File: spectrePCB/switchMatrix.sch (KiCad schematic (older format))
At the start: 259 parts, among them U2 ADG633YRU

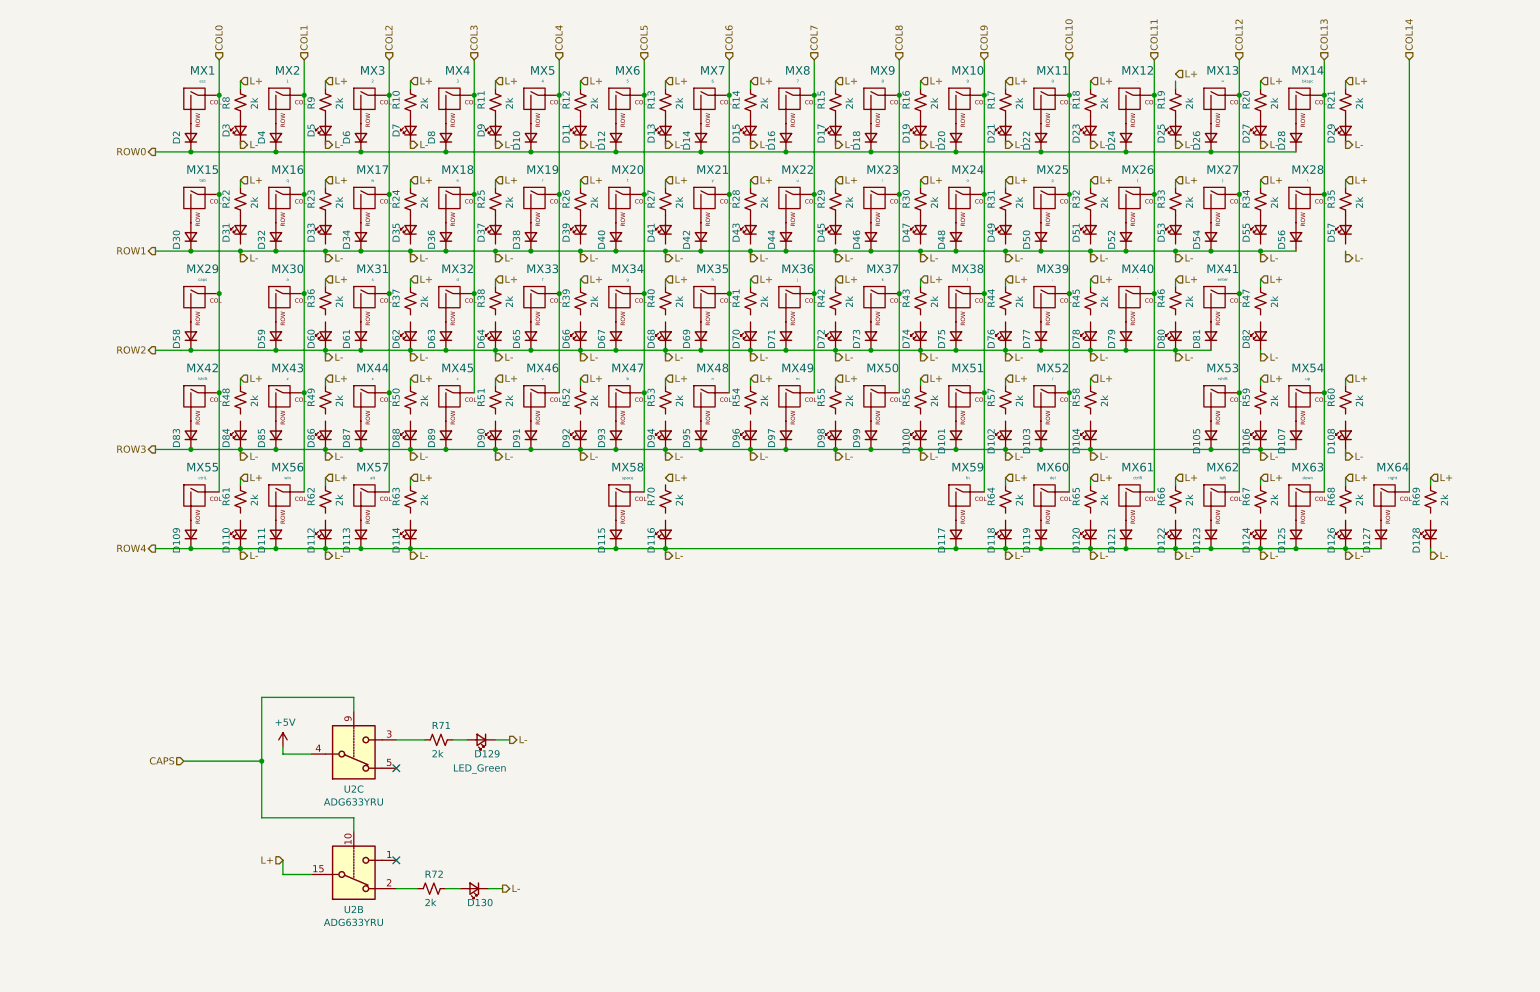
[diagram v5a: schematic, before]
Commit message: finished routing pcb
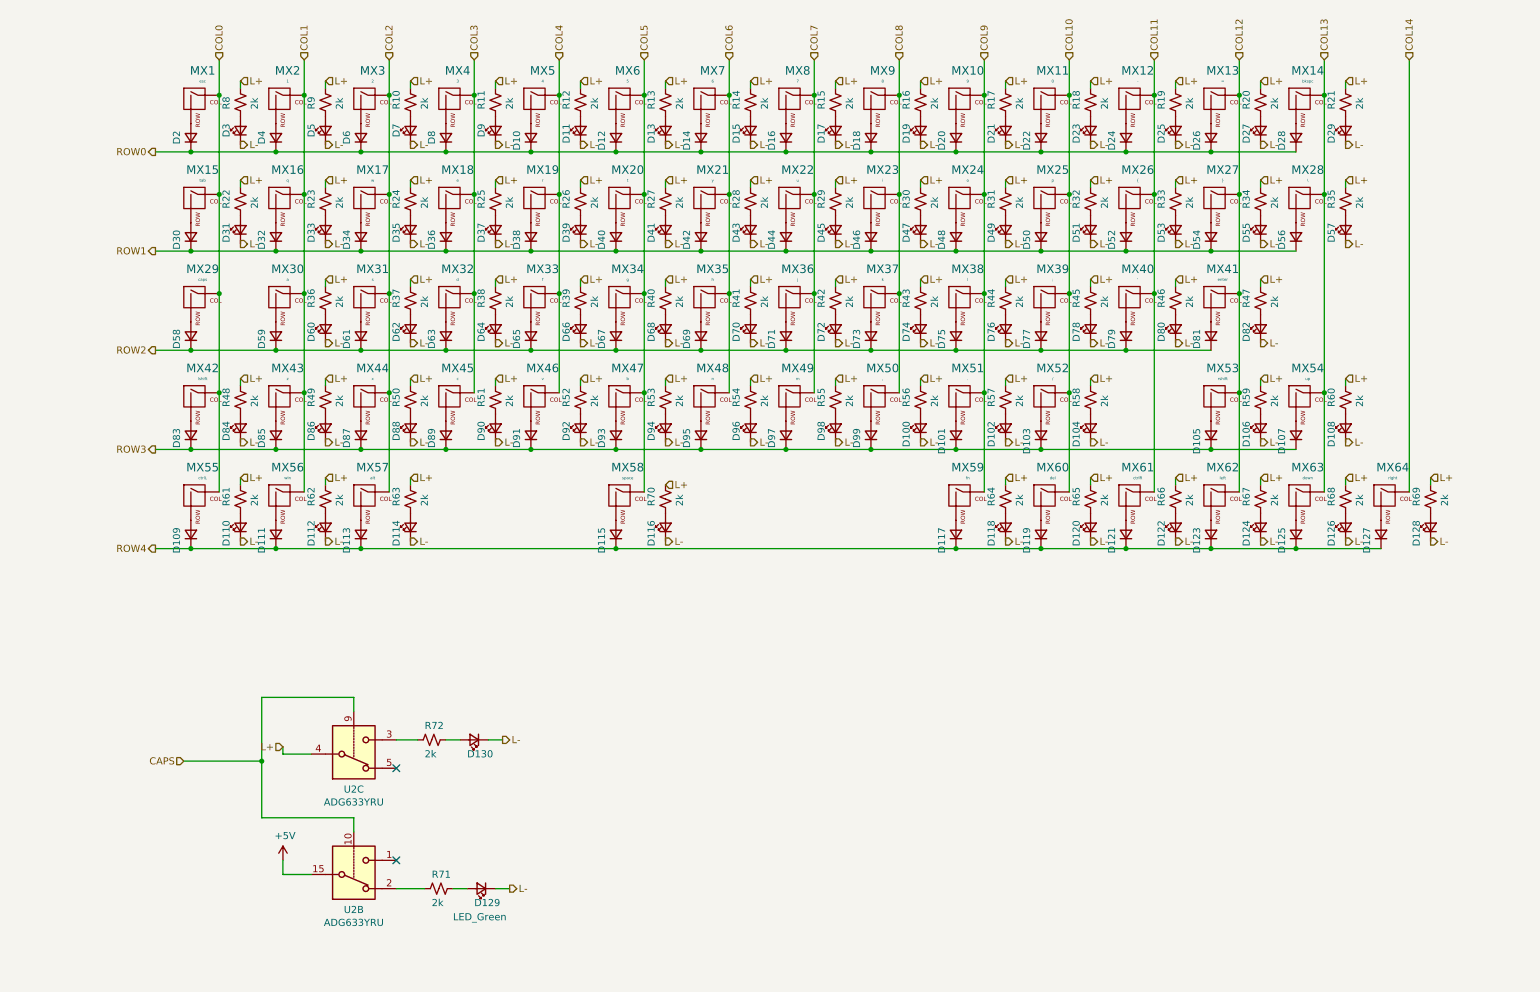
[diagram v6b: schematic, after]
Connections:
- net +5V: now also U2.15; no longer U2.4
- net L+: now also R19.1, R70.1, U2.4; no longer U2.15
- net L-: now also D31.1 (K), D33.1 (K), D35.1 (K), D37.1 (K), D39.1 (K), D41.1 (K), D43.1 (K), D45.1 (K), D47.1 (K), D49.1 (K), D51.1 (K), D53.1 (K), D55.1 (K), D57.1 (K); no longer D101.1 (K), D103.1 (K), D105.1 (K), D107.1 (K), D109.1 (K), D111.1 (K), D113.1 (K), D115.1 (K), D117.1 (K), D119.1 (K), D121.1 (K), D123.1 (K), D125.1 (K), D127.1 (K), D30.1 (K), D32.1 (K), D34.1 (K), D36.1 (K), D38.1 (K), D40.1 (K), D42.1 (K), D44.1 (K), D46.1 (K), D48.1 (K), D50.1 (K), D52.1 (K), D54.1 (K), D56.1 (K), D58.1 (K), D59.1 (K), D61.1 (K), D63.1 (K), D65.1 (K), D67.1 (K), D69.1 (K), D71.1 (K), D73.1 (K), D75.1 (K), D77.1 (K), D79.1 (K), D81.1 (K), D83.1 (K), D85.1 (K), D87.1 (K), D89.1 (K), D91.1 (K), D93.1 (K), D95.1 (K), D97.1 (K), D99.1 (K)
- net at R71.2: now also U2.2; no longer U2.3
- net at R72.2: now also U2.3; no longer U2.2
- net at D84.2 (A): now also R48.2
- net at D110.2 (A): now also R61.2
- net at D60.2 (A): now also R36.2
- net at D86.2 (A): now also R49.2
- net at D112.2 (A): now also R62.2
- net at D62.2 (A): now also R37.2
- net at D88.2 (A): now also R50.2
- net at D114.2 (A): now also R63.2
- net at D64.2 (A): now also R38.2
- net at D90.2 (A): now also R51.2
- net at D66.2 (A): now also R39.2
- net at D92.2 (A): now also R52.2
- net at D68.2 (A): now also R40.2
- net at D94.2 (A): now also R53.2
- net at D70.2 (A): now also R41.2
- net at D96.2 (A): now also R54.2
- net at D116.2 (A): now also R70.2
- net at D72.2 (A): now also R42.2
- net at D98.2 (A): now also R55.2
- net at D74.2 (A): now also R43.2
- net at D100.2 (A): now also R56.2
- net at D76.2 (A): now also R44.2
- net at D102.2 (A): now also R57.2
- net at D78.2 (A): now also R45.2
- net at D104.2 (A): now also R58.2
- net at D118.2 (A): now also R64.2
- net at D80.2 (A): now also R46.2
- net at D120.2 (A): now also R65.2
- net at D82.2 (A): now also R47.2
- net at D106.2 (A): now also R59.2
- net at D122.2 (A): now also R66.2
- net at D124.2 (A): now also R67.2
- net at D108.2 (A): now also R60.2
- net at D126.2 (A): now also R68.2
- net at D128.2 (A): now also R69.2
- new net ROW1: D30.1 (K), D32.1 (K), D34.1 (K), D36.1 (K), D38.1 (K), D40.1 (K), D42.1 (K), D44.1 (K), D46.1 (K), D48.1 (K), D50.1 (K), D52.1 (K), D54.1 (K), D56.1 (K)
- new net ROW2: D58.1 (K), D59.1 (K), D61.1 (K), D63.1 (K), D65.1 (K), D67.1 (K), D69.1 (K), D71.1 (K), D73.1 (K), D75.1 (K), D77.1 (K), D79.1 (K), D81.1 (K)
- new net ROW3: D101.1 (K), D103.1 (K), D105.1 (K), D107.1 (K), D83.1 (K), D85.1 (K), D87.1 (K), D89.1 (K), D91.1 (K), D93.1 (K), D95.1 (K), D97.1 (K), D99.1 (K)
- new net ROW4: D109.1 (K), D111.1 (K), D113.1 (K), D115.1 (K), D117.1 (K), D119.1 (K), D121.1 (K), D123.1 (K), D125.1 (K), D127.1 (K)
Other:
- moved on the sheet: D100, D102, D104, D106, D108, D110, D112, D114, D116, D118, D120, D122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
